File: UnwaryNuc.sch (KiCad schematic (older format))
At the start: 164 parts, among them J1 USB_B_Micro, J2 USB_A_Dual, J3 Conn_01x06_Male, J4 RJ45_Amphenol_RJMG1BD3B8K1ANR, J5 RJ45_Amphenol_RJMG1BD3B8K1ANR, Q1 2N3904, Q2 BC856BDW1, SW1 SW_SPST, U1 NUC980DF71YC, U2 LAN8740A-EN-TR, U3 LAN8740A-EN-TR, U4 LD3985M18R_TSOT23, U5 MIC4690, U6 LM3880, U7 AP2127K-1.2, Y1 ABS07-166, Y2 NX5032GA

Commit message: pushing up to pull to desktop
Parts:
- added R? (x6): 10k, Resistor_SMD:R_0603_1608Metric_Pad1.05x0.95mm_HandSolder, symbol Device:R
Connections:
- net labels added: BTSEL0, BTSEL1, FLASHCFG0, FLASHCFG1, JTAG.TCK, JTAG.TDI, JTAG.TDO, JTAG.TMS, JTAG.TRST, QSPI0_CLK, QSPI0_MISO0, QSPI0_MISO1, QSPI0_MOSI0, QSPI0_MOSI1, QSPI0_SS0, UART_DBG_EN, WDT_DISABLE
- wire segments 571 -> 594
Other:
- moved on the sheet: C?, R11, R12, R13, R14

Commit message: updating deprecated library footprints. Sch/pcb back in sync on new system
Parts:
- C1, C10, C11, C12, C13, C14, C15, C16, C17, C18, C19, C2, C20, C21, C27, C28, C29, C30, C31, C32, C33, C34, C35, C36, C37, C4, C5, C6, C7, C8, C9: footprint Capacitor_SMD:C_1206_3216Metric_Pad1.42x1.75mm_HandSolder -> Capacitor_SMD:C_1206_3216Metric_Pad1.33x1.80mm_HandSolder
- C22, C23, C24, C3: footprint Capacitor_SMD:C_0603_1608Metric_Pad1.05x0.95mm_HandSolder -> Capacitor_SMD:C_0603_1608Metric_Pad1.08x0.95mm_HandSolder
- C38, C39, C40, C45, C46, C47, C48, C49, C50, C51: renamed from C?; footprint Capacitor_SMD:C_0603_1608Metric_Pad1.05x0.95mm_HandSolder -> Capacitor_SMD:C_0603_1608Metric_Pad1.08x0.95mm_HandSolder
- C41, C42, C43, C44: renamed from C?; footprint Capacitor_SMD:C_1206_3216Metric_Pad1.42x1.75mm_HandSolder -> Capacitor_SMD:C_1206_3216Metric_Pad1.33x1.80mm_HandSolder
- C52, C53: renamed from C?; footprint Capacitor_SMD:C_0805_2012Metric_Pad1.15x1.40mm_HandSolder -> Capacitor_SMD:C_0805_2012Metric_Pad1.18x1.45mm_HandSolder
- J1: symbol Connector:USB_B_Micro -> UnwaryNuc-rescue:USB_B_Micro-Connector
- J2: symbol Connector_Unwary:USB_A_Dual -> UnwaryNuc-rescue:USB_A_Dual-Connector_Unwary
- R1, R10, R2, R3, R4, R5, R6, R7, R8, R9: footprint Resistor_SMD:R_0805_2012Metric_Pad1.15x1.40mm_HandSolder -> Resistor_SMD:R_0805_2012Metric_Pad1.20x1.40mm_HandSolder
- R11, R12, R13, R14, R15, R16, R17, R18, R19, R20, R21, R22, R23, R24, R26, R27, R28, R29, R30, R31, R32, R33, R34, R35, R36, R37, R38, R39, R40, R41, R42, R43, R44, R45, R46, R47, R48, R49, R50, R51, R52, R53: footprint Resistor_SMD:R_0603_1608Metric_Pad1.05x0.95mm_HandSolder -> Resistor_SMD:R_0603_1608Metric_Pad0.98x0.95mm_HandSolder
- R25, R54, R55, R56, R57, R58, R59, R60, R61, R62, R63, R64, R65, R66, R67, R68, R69, R70, R73, R74, R75, R76, R77, R78, R79, R80, R81, R82, R83, R84, R85, R86: renamed from R?; footprint Resistor_SMD:R_0603_1608Metric_Pad1.05x0.95mm_HandSolder -> Resistor_SMD:R_0603_1608Metric_Pad0.98x0.95mm_HandSolder
- R71, R72: renamed from R?; footprint Resistor_SMD:R_0805_2012Metric_Pad1.15x1.40mm_HandSolder -> Resistor_SMD:R_0805_2012Metric_Pad1.20x1.40mm_HandSolder
- U2, U3: symbol 2020-12-18_02-56-37:LAN8740A-EN-TR -> UnwaryNuc-rescue:LAN8740A-EN-TR-2020-12-18_02-56-37
- U7: symbol Regulator_Linear:AP2127K-1.2 -> UnwaryNuc-rescue:AP2127K-1.2-Regulator_Linear
- gave numbers to parts that had none: 5

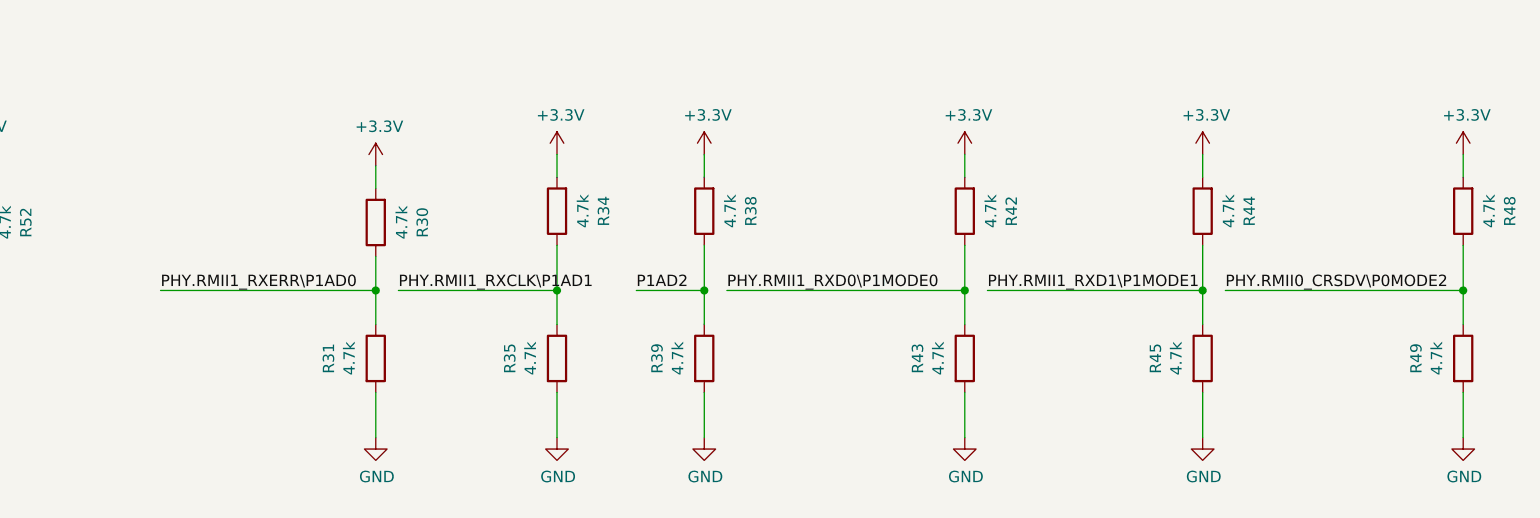
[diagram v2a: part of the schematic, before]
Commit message: Some rough placement grouping and power routing
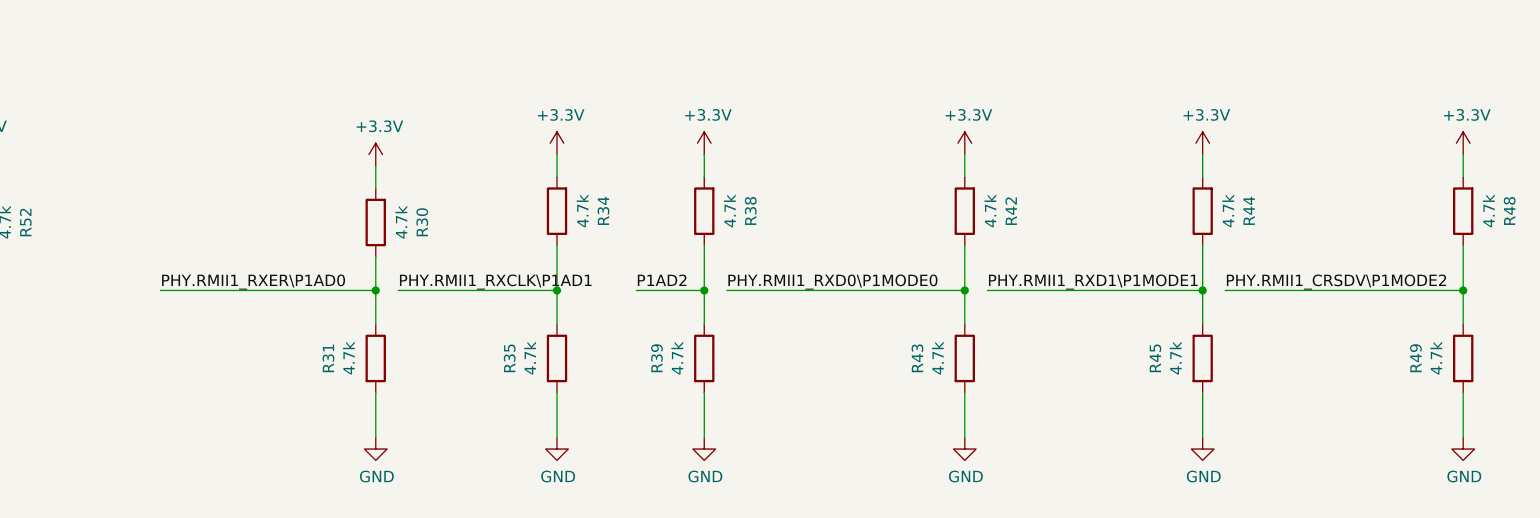
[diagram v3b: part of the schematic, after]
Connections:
- net labels removed: PHY.RMII1_RXERR\P1AD0
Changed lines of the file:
@@
 Connection ~ 24900 2200
 Text Label 25950 18150 0    50   ~ 0
-PHY.RMII1_RXERR\P1AD0
+PHY.RMII1_RXER\P1AD0
 Wire Wire Line
 	25950 18150 26900 18150
@@
 	31700 17950 31700 18150
 Text Label 30650 18150 0    50   ~ 0
-PHY.RMII0_CRSDV\P0MODE2
+PHY.RMII1_CRSDV\P1MODE2
 Wire Wire Line
 	30650 18150 31700 18150

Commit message: added QSPI for boot, routed 1 phy, more placement completed
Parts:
- added C54, C55: 0.1u, Capacitor_SMD:C_1206_3216Metric_Pad1.33x1.80mm_HandSolder, symbol Device:C
- added J6: Conn_02x04_Odd_Even, Connector_PinHeader_2.54mm:PinHeader_2x04_P2.54mm_Vertical, symbol Connector_Generic:Conn_02x04_Odd_Even
- added U8: S25FL127SABMFV100, UnwaryNuc:S25FL127SABMFV100, symbol Cypress_SPI:S25FL127SABMFV100
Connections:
- net labels added: P0.0N, P0.0P, P0.1N, P0.1P, P1.0N, P1.0P, P1.1N, P1.1P, QSPI0_SS1
- wire segments 594 -> 559
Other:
- moved on the sheet: U1

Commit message: started other phy
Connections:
- wire segments 559 -> 618
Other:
- moved on the sheet: U1
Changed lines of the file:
@@
 $EndDescr
 $Comp
-L UnwaryNuc:NUC980DF71YC U1
-U 1 1 5FE0DCCB
-P 11350 6500
-F 0 "U1" H 14750 5312 197 0000 C CNN
-F 1 "NUC980DF71YC" H 14750 5000 197 0000 C CNN
-F 2 "UnwaryNuc:NUC980DF71YC" H 13500 3300 50  0001 C CNN
-F 3 "" H 13500 3300 50  0001 C CNN
-	1    11350 6500
-	1    0    0    1
-$EndComp
-$Comp
 L UnwaryNuc-rescue:LAN8740A-EN-TR-2020-12-18_02-56-37 U3
 U 1 1 5FE1B976
@@
 Text Label 7500 8550 2    50   ~ 0
 VDD_RTC
-Wire Wire Line
-	18250 3800 18250 3750
 $Comp
 L power:+3.3V #PWR011
@@
 	12600 2800 12600 3350
 Wire Wire Line
-	18250 4100 18250 4150
-Wire Wire Line
 	18000 3800 18250 3800
 Connection ~ 18000 3800
@@
 Text Label 27200 6650 0    50   ~ 0
 P1.1N
-Connection ~ 18250 3750
 Wire Wire Line
-	18250 3750 18250 3700
-Connection ~ 11250 4100
-Connection ~ 11250 3800
+	16200 5200 16250 5200
+Connection ~ 16550 5200
+Wire Wire Line
+	16550 5200 16650 5200
+Wire Wire Line
+	16450 5200 16550 5200
+Connection ~ 16450 5200
+Connection ~ 16350 5200
+Wire Wire Line
+	16350 5200 16450 5200
+Wire Wire Line
+	16250 5200 16350 5200
+Connection ~ 16250 5200
+Connection ~ 16150 5200
+Wire Wire Line
+	16150 5200 16200 5200
+Wire Wire Line
+	16050 5200 16150 5200
+Connection ~ 16050 5200
+Connection ~ 15950 5200
+Wire Wire Line
+	15950 5200 16050 5200
+Wire Wire Line
+	15850 5200 15950 5200
+Wire Wire Line
+	14600 15100 14650 15100
+Connection ~ 16550 15100
+Wire Wire Line
+	16550 15100 16650 15100
+Wire Wire Line
+	16450 15100 16550 15100
+Connection ~ 16450 15100
+Connection ~ 16350 15100
+Wire Wire Line
+	16350 15100 16450 15100
+Wire Wire Line
+	16250 15100 16350 15100
+Connection ~ 16250 15100
+Connection ~ 16150 15100
+Wire Wire Line
+	16150 15100 16250 15100
+Wire Wire Line
+	16050 15100 16150 15100
+Connection ~ 16050 15100
+Connection ~ 15950 15100
+Wire Wire Line
+	15950 15100 16050 15100
+Wire Wire Line
+	15850 15100 15950 15100
+Connection ~ 15850 15100
+Connection ~ 15750 15100
+Wire Wire Line
+	15750 15100 15850 15100
+Wire Wire Line
+	15650 15100 15750 15100
+Connection ~ 15650 15100
+Connection ~ 15550 15100
+Wire Wire Line
+	15550 15100 15650 15100
+Wire Wire Line
+	15450 15100 15550 15100
+Connection ~ 15450 15100
+Connection ~ 15350 15100
+Wire Wire Line
+	15350 15100 15450 15100
+Wire Wire Line
+	15250 15100 15350 15100
+Connection ~ 15250 15100
+Connection ~ 15150 15100
+Wire Wire Line
+	15150 15100 15250 15100
+Wire Wire Line
+	15050 15100 15150 15100
+Connection ~ 15050 15100
+Connection ~ 14950 15100
+Wire Wire Line
+	14950 15100 15050 15100
+Wire Wire Line
+	14850 15100 14950 15100
+Connection ~ 14850 15100
+Connection ~ 14750 15100
+Wire Wire Line
+	14750 15100 14850 15100
+Wire Wire Line
+	14650 15100 14750 15100
+Connection ~ 14650 15100
+Connection ~ 14550 15100
+Wire Wire Line
+	14550 15100 14600 15100
 Wire Wire Line
-	14250 5200 14500 5200
+	14450 15100 14550 15100
+Connection ~ 14450 15100
+Connection ~ 14350 15100
 Wire Wire Line
-	18250 13200 18250 13600
+	14350 15100 14450 15100
 Wire Wire Line
-	18250 12850 18250 13200
+	14250 15100 14350 15100
+Connection ~ 14250 15100
+Connection ~ 14150 15100
 Wire Wire Line
-	12850 5200 13300 5200
+	14150 15100 14250 15100
 Wire Wire Line
-	13300 5200 13850 5200
+	14050 15100 14150 15100
+Connection ~ 14050 15100
+Connection ~ 13950 15100
 Wire Wire Line
-	14500 5200 14850 5200
+	13950 15100 14050 15100
 Wire Wire Line
-	15850 5200 16200 5200
+	13850 15100 13950 15100
+Connection ~ 13850 15100
+Connection ~ 13750 15100
 Wire Wire Line
-	16200 5200 16650 5200
+	13750 15100 13850 15100
 Wire Wire Line
-	14600 15100 16650 15100
+	13650 15100 13750 15100
+Connection ~ 13650 15100
+Connection ~ 13550 15100
 Wire Wire Line
-	12850 15100 14600 15100
+	13550 15100 13650 15100
+Wire Wire Line
+	13450 15100 13550 15100
+Connection ~ 13450 15100
+Connection ~ 13350 15100
+Wire Wire Line
+	13350 15100 13450 15100
+Wire Wire Line
+	13250 15100 13350 15100
+Connection ~ 13250 15100
+Connection ~ 13150 15100
+Wire Wire Line
+	13150 15100 13250 15100
+Wire Wire Line
+	13050 15100 13150 15100
+Connection ~ 13050 15100
+Connection ~ 12950 15100
+Wire Wire Line
+	12950 15100 13050 15100
+Wire Wire Line
+	12850 15100 12950 15100
+Connection ~ 18250 14250
+Connection ~ 18250 13500
+Wire Wire Line
+	18250 13200 18250 12950
+Wire Wire Line
+	18250 12950 18250 12850
+Connection ~ 18250 12950
+Wire Wire Line
+	18250 13500 18250 13200
+Wire Wire Line
+	18250 13600 18250 13500
+Connection ~ 18250 12100
+Connection ~ 18250 11800
+Connection ~ 14750 5200
+Wire Wire Line
+	14750 5200 14850 5200
+Wire Wire Line
+	14650 5200 14750 5200
+Connection ~ 14650 5200
+Connection ~ 14550 5200
+Wire Wire Line
+	14550 5200 14650 5200
+Wire Wire Line
+	14500 5200 14550 5200
+Wire Wire Line
+	14350 5200 14250 5200
+Connection ~ 14350 5200
+Connection ~ 14450 5200
+Wire Wire Line
+	14450 5200 14350 5200
+Wire Wire Line
+	14500 5200 14450 5200
+Connection ~ 13750 5200
+Wire Wire Line
+	13750 5200 13850 5200
+Wire Wire Line
+	13650 5200 13750 5200
+Connection ~ 13650 5200
+Connection ~ 13550 5200
+Wire Wire Line
+	13550 5200 13650 5200
+Wire Wire Line
+	13450 5200 13550 5200
+Connection ~ 13450 5200
+Connection ~ 13350 5200
+Wire Wire Line
+	13350 5200 13450 5200
+Wire Wire Line
+	13300 5200 13350 5200
+Connection ~ 13250 5200
+Wire Wire Line
+	13150 5200 13050 5200
+Connection ~ 13150 5200
+Connection ~ 13050 5200
+Wire Wire Line
+	13050 5200 12950 5200
+Wire Wire Line
+	12950 5200 12850 5200
+Connection ~ 12950 5200
+Wire Wire Line
+	13250 5200 13150 5200
+Wire Wire Line
+	13300 5200 13250 5200
+Wire Wire Line
+	18250 3800 18250 3700
+Wire Wire Line
+	18250 4100 18250 4350
+$Comp
+L UnwaryNuc:NUC980DF71YC U1
+U 1 1 5FE0DCCB
+P 11350 6500
+F 0 "U1" H 14750 5312 197 0000 C CNN
+F 1 "NUC980DF71YC" H 14750 5000 197 0000 C CNN
+F 2 "UnwaryNuc:NUC980DF71YC" H 13500 3300 50  0001 C CNN
+F 3 "" H 13500 3300 50  0001 C CNN
+	1    11350 6500
+	1    0    0    -1
+$EndComp
 $EndSCHEMATC

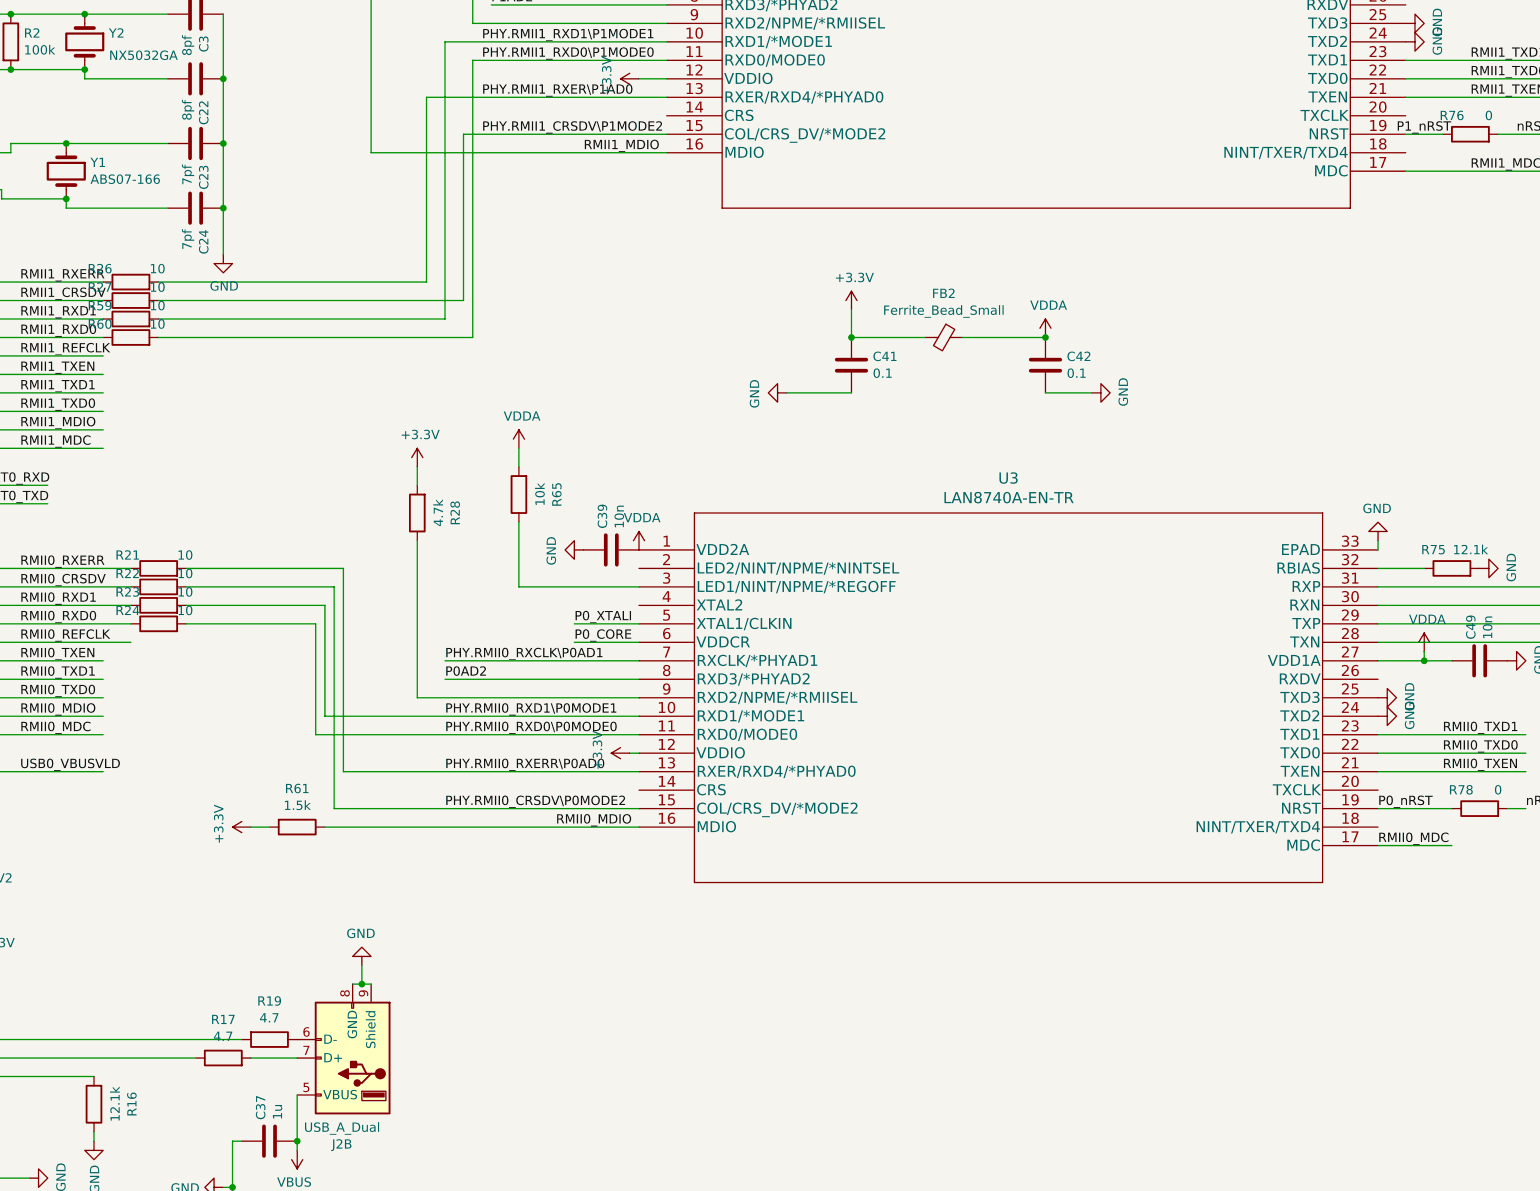
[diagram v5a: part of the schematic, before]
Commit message: Signal routing pretty much done, working out power distribution. Still could/should add Headers for other I/O, and an ESP backpack or something
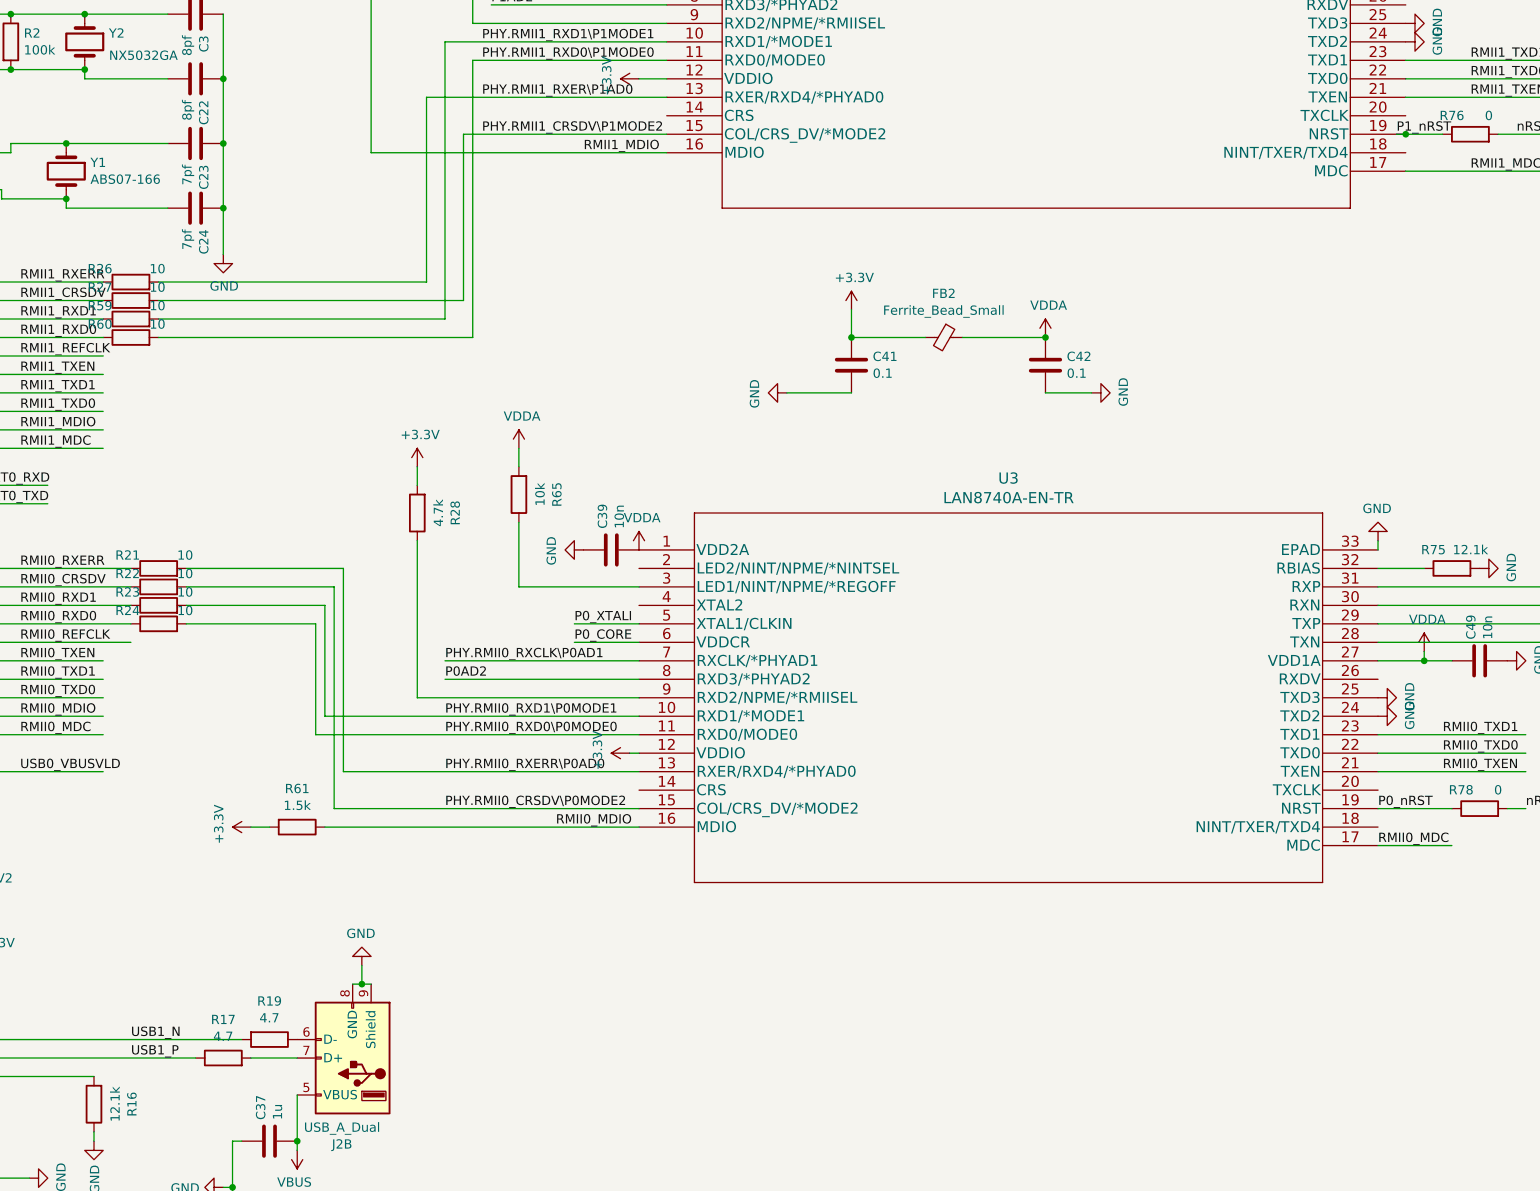
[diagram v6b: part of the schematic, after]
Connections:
- net labels added: USB1_N, USB1_P
- wire segments 618 -> 619
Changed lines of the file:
@@
 	1    0    0    -1
 $EndComp
+Wire Wire Line
+	26050 7550 26100 7550
+Connection ~ 26100 7550
+Text Label 19200 12450 0    50   ~ 0
+USB1_N
+Text Label 19200 12550 0    50   ~ 0
+USB1_P
 $EndSCHEMATC
